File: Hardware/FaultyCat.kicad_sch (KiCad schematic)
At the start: 74 parts, among them J1 Antenna, J2 BG306-02-A-2-0400-L-G, J3 Header7, J4 Header 2, J5 Header 4, J6 Input Power:2x AA Battery, P1 USB_C_Plug_USB2.0, Q1 AO3422, Q1 DMG3415U-7, Q2 AO3422, Q3 LDA111STR, Q4 RGT16BM65DTL, SW1 TL3305AF260QG, SW2 ON, SW3 TL3305AF260QG, SW4 RESET, SW5 BOOT, SW6 TL3305AF260QG, T1 ATB322524, T2 ATB322524, U1 AP2112K-3.3, U2 W25Q16JV, U3 RP2040, Y1 12Mhz

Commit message: feat: init faultycat 2
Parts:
- removed J3: Header7, Connector_PinHeader_2.54mm:PinHeader_1x07_P2.54mm_Vertical, symbol Connector_Generic:Conn_01x07
- added D11: LED, symbol Device:LED
- added J3: Output Mosfet, symbol Connector_Generic:Conn_01x02
- added J7: Conn_01x10, symbol Connector_Generic:Conn_01x10
- added J8: External Source, symbol Connector_Generic:Conn_01x02
- added Q6: NMOS, symbol Simulation_SPICE:NMOS
- added R15: 10K, symbol Device:R_Small
- added R21: 1K8, symbol Device:R_Small
- added R22: 100, symbol Device:R_Small
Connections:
- net GND: now also D11.1 (K), J7.10 (Pin_10), J8.2 (Pin_2), Q6.3 (S), R15.2
- net GP0: now also J7.1 (Pin_1)
- net GP1: now also J7.2 (Pin_2)
- net GP2: now also J7.3 (Pin_3)
- net GP3: now also J7.4 (Pin_4)
- net GP4: now also J7.5 (Pin_5)
- net GP5: now also J7.6 (Pin_6)
- net GP6: now also J7.7 (Pin_7); no longer R13.2
- net GP7: now also J7.8 (Pin_8); no longer R14.2
- net GP8: now reaches U3.11 (GPIO8)
- net GP8: now also J7.9 (Pin_9)
- net GP9: now reaches U3.12 (GPIO9)
- net GP9: now also R13.2
- net GP10: now reaches U3.13 (GPIO10)
- net GP10: now also R14.2
- net GP12: now reaches U3.15 (GPIO12)
- net GP12: now also R22.1
- new net: J3.1 (Pin_1), Q6.1 (D)
- new net: Q6.2 (G), R15.1, R21.1, R22.2
- new net: D11.2 (A), R21.2
- new net: J3.2 (Pin_2), J8.1 (Pin_1)
- no-connect marks 17 -> 13
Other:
- note added: "Fault Injection"
- note added: "MOSFET Glitch"
- note added: "blueTag"
- company: (none) -> Electronic Cats
- title: (none) -> FaultyCat
- moved on the sheet: D7, D8, R13, R14, SW3

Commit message: feat(Hw):Init_Floorplan
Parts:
- removed D11: LED, symbol Device:LED
- removed J3: Output Mosfet, symbol Connector_Generic:Conn_01x02
- removed J8: External Source, symbol Connector_Generic:Conn_01x02
- removed Q6: NMOS, symbol Simulation_SPICE:NMOS
- removed R15: 10K, symbol Device:R_Small
- removed R21: 1K8, symbol Device:R_Small
- removed R22: 100, symbol Device:R_Small
- added Q7: IRLML2502, Package_TO_SOT_SMD:SOT-23, symbol pico-glitcher:NMOSFETSOT23-GSD
- added Q8: IRF7807PBF, BuggyCat:SOIC-8_SI, symbol pico-glitcher:MOSFET-NCHANNEL-SOIC8
- added R23, R24: 1R, Resistor_SMD:R_0603_1608Metric, symbol Device:R
- added R25, R26: 10K, Resistor_SMD:R_0603_1608Metric, symbol Device:R
- added X1: BU-SMA, BuggyCat:SMA-KE901, symbol pico-glitcher:BU-SMA-V
- added X_GLITCH1: PINHDR_1X1, Connector_PinHeader_2.54mm:PinHeader_1x01_P2.54mm_Vertical, symbol Connector:Conn_01x01_Pin
- J7: footprint (none) -> Connector_PinSocket_2.54mm:PinSocket_1x10_P2.54mm_Vertical
- R17: LCSC# C99198 -> C103199
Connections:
- net GND: now also Q7.2 (S), Q8.1 (S@1), Q8.2 (S@2), Q8.3 (S@3), R25.2, R26.1, X1.2, X1.3 (2), X1.4 (2), X1.5 (2)
- net HPGLITCH2: now reaches U3.27 (GPIO16)
- net HPGLITCH2: now also R24.1
- net LPGLITCH2: now reaches U3.28 (GPIO17)
- net LPGLITCH2: now also R23.2
- net GP12: no longer names the net of U3.15 (GPIO12)
- new net: Q7.1 (G), R23.1, R25.1
- new net: Q8.4 (G), R24.2, R26.2
- new net: Q7.3 (D), Q8.5 (D@4), Q8.6 (D@3), Q8.7 (D@2), Q8.8 (D@1), X1.1, X_GLITCH1.1 (Pin_1)
- no-connect marks 13 -> 12

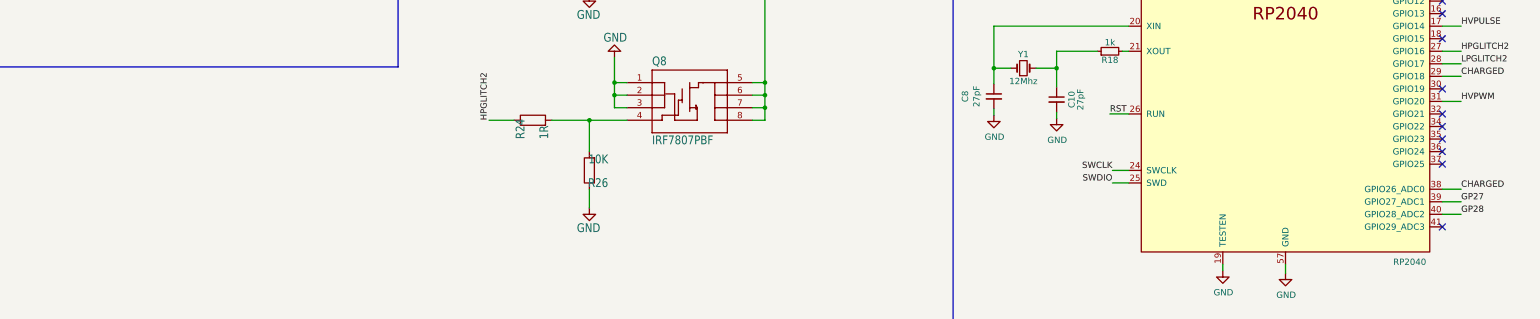
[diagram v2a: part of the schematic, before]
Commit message: feat(Hw):Update_Route_And_Schematic
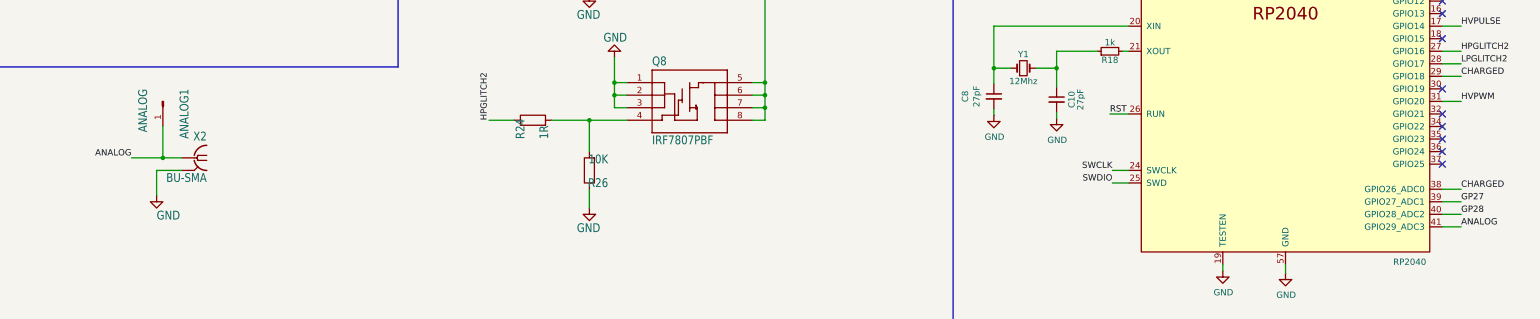
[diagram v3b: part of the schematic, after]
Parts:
- added ANALOG1: ANALOG, Connector_PinHeader_2.54mm:PinHeader_1x01_P2.54mm_Vertical, symbol Connector:Conn_01x01_Pin
- added X2: BU-SMA, BuggyCat:SMA-KE901, symbol pico-glitcher:BU-SMA-V
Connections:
- net GND: now also X2.2, X2.3 (2), X2.4 (2), X2.5 (2)
- net ANALOG: now reaches U3.41 (GPIO29_ADC3)
- net ANALOG: now also ANALOG1.1 (Pin_1), X2.1
- no-connect marks 12 -> 11

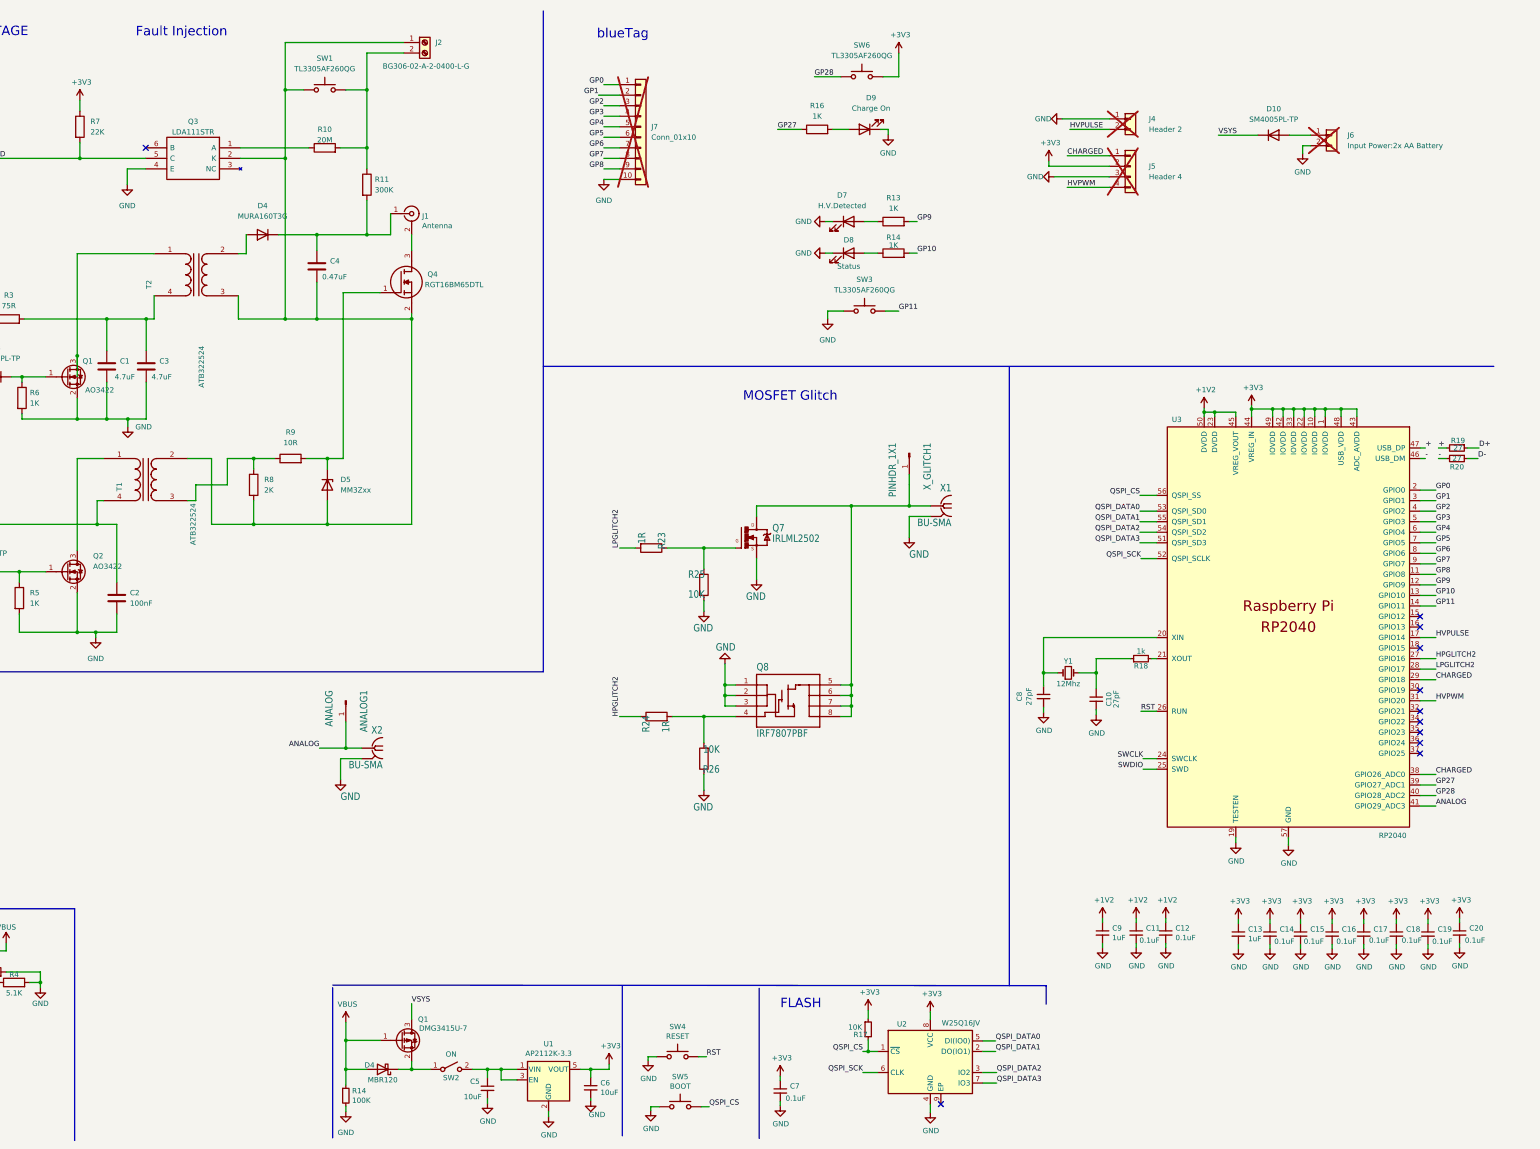
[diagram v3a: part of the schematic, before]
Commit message: feat(hw): add shift level in schematic
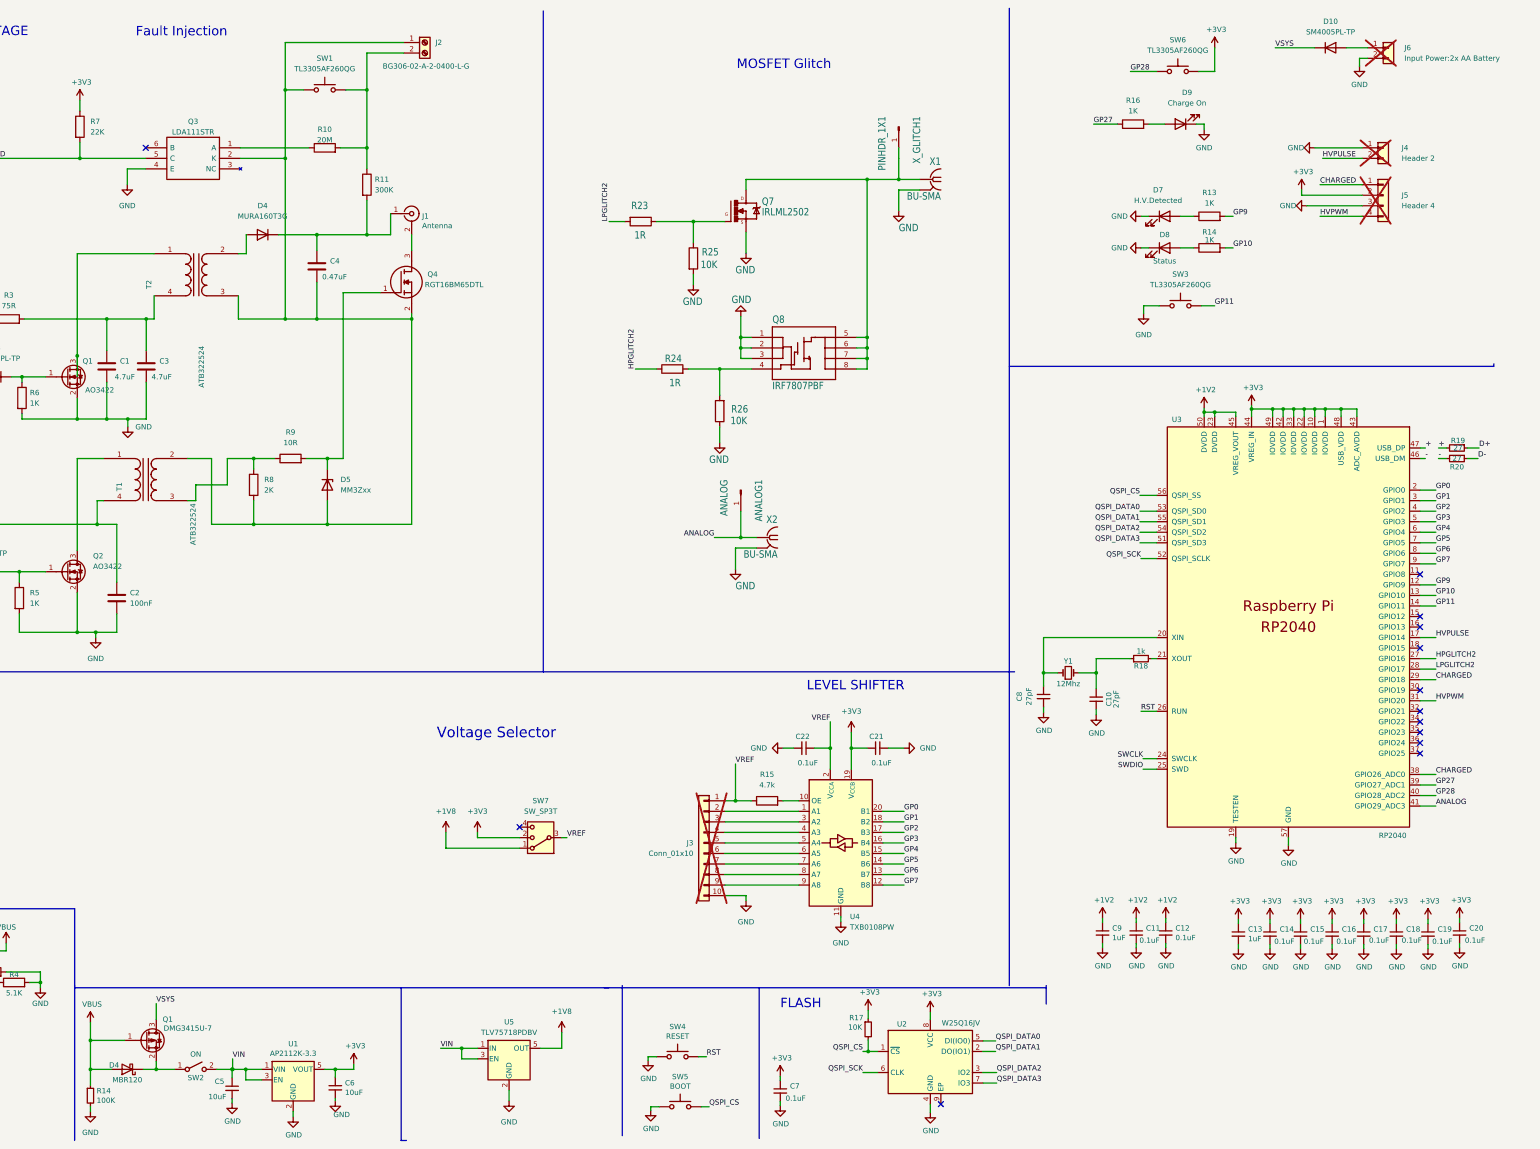
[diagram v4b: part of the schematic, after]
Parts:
- removed J7: Conn_01x10, Connector_PinSocket_2.54mm:PinSocket_1x10_P2.54mm_Vertical, symbol Connector_Generic:Conn_01x10
- added C21, C22: 0.1uF, Capacitor_SMD:C_0603_1608Metric, symbol Device:C_Small
- added J3: Conn_01x10, Connector_PinSocket_2.54mm:PinSocket_1x10_P2.54mm_Vertical, symbol Connector_Generic:Conn_01x10
- added R15: 4.7k, Resistor_SMD:R_0603_1608Metric, symbol Device:R
- added SW7: SW_SP3T, symbol Switch:SW_SP3T
- added U4: TXB0108PW, Package_SO:TSSOP-20_4.4x6.5mm_P0.65mm, symbol Logic_LevelTranslator:TXB0108PW
- added U5: TLV75718PDBV, Package_TO_SOT_SMD:SOT-23-5, symbol Regulator_Linear:TLV75718PDBV
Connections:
- net +3V3: now also C21.2, SW7.2, U4.19 (V_{CCB})
- net GND: now also C21.1, C22.2, J3.10 (Pin_10), U4.11 (GND), U5.2 (GND)
- net GP0: now also U4.20 (B1)
- net GP1: now also U4.18 (B2)
- net GP2: now also U4.17 (B3)
- net GP3: now also U4.16 (B4)
- net GP4: now also U4.15 (B5)
- net GP5: now also U4.14 (B6)
- net GP6: now also U4.13 (B7)
- net GP7: now also U4.12 (B8)
- net VIN: now reaches C5.1, SW2.2 (B), U1.1 (VIN), U1.3 (EN)
- net VIN: now also U5.1 (IN), U5.3 (EN)
- net GP8: no longer names the net of U3.11 (GPIO8)
- new net: J3.2 (Pin_2), U4.1 (A1)
- new net: J3.3 (Pin_3), U4.3 (A2)
- new net: J3.4 (Pin_4), U4.4 (A3)
- new net: J3.5 (Pin_5), U4.5 (A4)
- new net: J3.6 (Pin_6), U4.6 (A5)
- new net: J3.7 (Pin_7), U4.7 (A6)
- new net: J3.8 (Pin_8), U4.8 (A7)
- new net: J3.9 (Pin_9), U4.9 (A8)
- new net: R15.2, U4.10 (OE)
- new net +1V8: SW7.1, U5.5 (OUT)
- new net VREF: C22.1, J3.1 (Pin_1), R15.1, SW7.3, U4.2 (V_{CCA})
- no-connect marks 11 -> 13
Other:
- note added: "LEVEL SHIFTER"
- note added: "Voltage Selector"
- note removed: "blueTag"
- moved on the sheet: ANALOG1, C5, C6, D10, D4, D7, D8, D9, J4, J5, J6, Q1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

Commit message: feat(hw): place level shifter on pcb
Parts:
- SW7: footprint (none) -> Button_Switch_SMD:SW_SP3T_PCM13
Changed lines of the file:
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@@
 			)
 		)
-		(property "Footprint" ""
+		(property "Footprint" "Button_Switch_SMD:SW_SP3T_PCM13"
 			(at 193.675 216.535 0)
 			(effects
